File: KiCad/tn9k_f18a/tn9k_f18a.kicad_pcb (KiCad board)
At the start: 2 copper layers, 27.9 x 88.3 mm, 9 parts, among them J1 Conn_01x20, J2 Conn_01x20, J3 Conn_01x24, J4 Conn_01x24, J5 Conn_02x04_Counter_Clockwise, J6 Conn_02x08_Odd_Even, U1 SN74LVC245, U2 SN74LVC245, U3 SN74LVC245

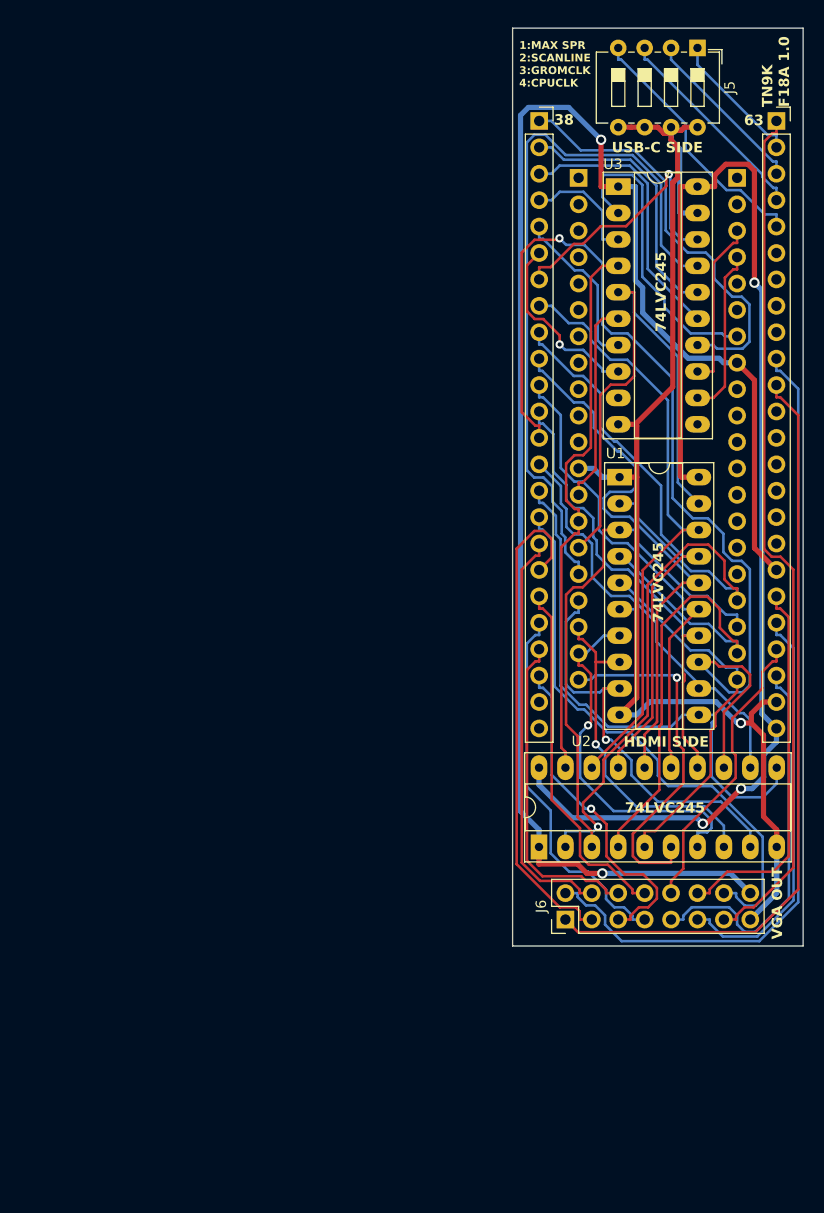
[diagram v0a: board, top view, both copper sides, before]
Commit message: SMD version
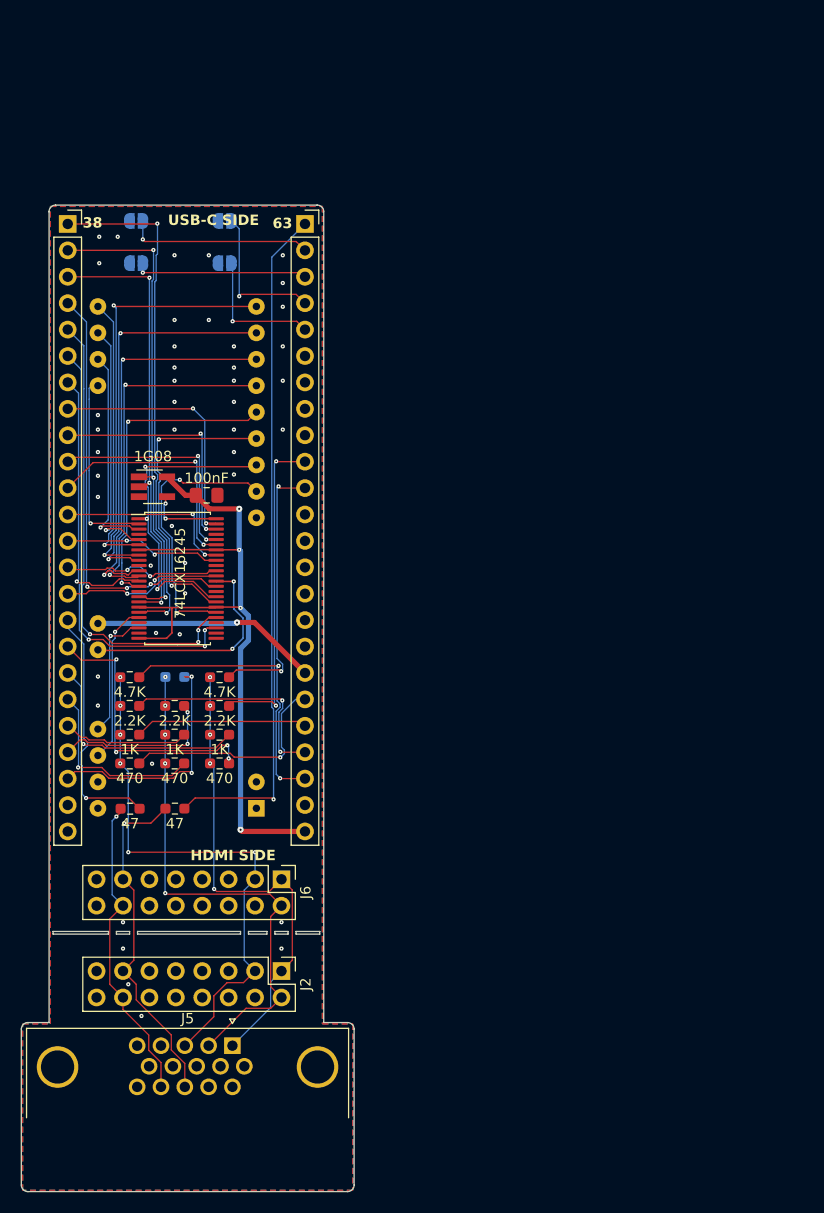
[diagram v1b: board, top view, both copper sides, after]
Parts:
- removed U2, U3: SN74LVC245, Package_DIP:DIP-20_W7.62mm_Socket_LongPads
- added C1: 100nF, Capacitor_SMD:C_0805_2012Metric_Pad1.18x1.45mm_HandSolder, F.Cu at (117.9, 86.2)
- added JP1: MAX SPR, Jumper:SolderJumper-2_P1.3mm_Open_RoundedPad1.0x1.5mm, B.Cu at (111.1, 59.8)
- added JP2: SCANLINE, Jumper:SolderJumper-2_P1.3mm_Open_RoundedPad1.0x1.5mm, B.Cu at (111.1, 63.9)
- added JP3: GROMCLK, Jumper:SolderJumper-2_P1.3mm_Open_RoundedPad1.0x1.5mm, B.Cu at (119.6, 59.8)
- added JP4: CPUCLK, Jumper:SolderJumper-2_P1.3mm_Open_RoundedPad1.0x1.5mm, B.Cu at (119.6, 63.9)
- added R1: 4.7K, Resistor_SMD:R_0603_1608Metric_Pad0.98x0.95mm_HandSolder, F.Cu at (119.1, 103.7)
- added R10: 2.2K, Resistor_SMD:R_0603_1608Metric_Pad0.98x0.95mm_HandSolder, F.Cu at (110.5, 106.5)
- added R11: 1K, Resistor_SMD:R_0603_1608Metric_Pad0.98x0.95mm_HandSolder, F.Cu at (110.5, 109.2)
- added R12: 470, Resistor_SMD:R_0603_1608Metric_Pad0.98x0.95mm_HandSolder, F.Cu at (110.5, 112.0)
- added R13: 47, Resistor_SMD:R_0603_1608Metric_Pad0.98x0.95mm_HandSolder, F.Cu at (114.8, 116.3)
- added R14: 47, Resistor_SMD:R_0603_1608Metric_Pad0.98x0.95mm_HandSolder, F.Cu at (110.5, 116.3)
- added R2: 2.2K, Resistor_SMD:R_0603_1608Metric_Pad0.98x0.95mm_HandSolder, F.Cu at (119.1, 106.5)
- added R3: 1K, Resistor_SMD:R_0603_1608Metric_Pad0.98x0.95mm_HandSolder, F.Cu at (119.1, 109.2)
- added R4: 470, Resistor_SMD:R_0603_1608Metric_Pad0.98x0.95mm_HandSolder, F.Cu at (119.1, 112.0)
- added R5: 4.7K, Resistor_SMD:R_0603_1608Metric_Pad0.98x0.95mm_HandSolder, B.Cu at (114.8, 103.7)
- added R6: 2.2K, Resistor_SMD:R_0603_1608Metric_Pad0.98x0.95mm_HandSolder, F.Cu at (114.8, 106.5)
- added R7: 1K, Resistor_SMD:R_0603_1608Metric_Pad0.98x0.95mm_HandSolder, F.Cu at (114.8, 109.2)
- added R8: 470, Resistor_SMD:R_0603_1608Metric_Pad0.98x0.95mm_HandSolder, F.Cu at (114.8, 112.0)
- added R9: 4.7K, Resistor_SMD:R_0603_1608Metric_Pad0.98x0.95mm_HandSolder, F.Cu at (110.5, 103.7)
- added U4: 74LCX16245, Package_SO:TSSOP-48_6.1x12.5mm_P0.5mm, F.Cu at (115.1, 94.2)
- J1: value Conn_01x20 -> ~; footprint Connector_PinHeader_2.54mm:PinHeader_1x20_P2.54mm_Vertical -> f18a_footprints:TMS99xxA_Replacement; moved to F.Cu
- J2: value Conn_01x20 -> VGA; footprint Connector_PinHeader_2.54mm:PinHeader_1x20_P2.54mm_Vertical -> Connector_PinHeader_2.54mm:PinHeader_2x08_P2.54mm_Vertical; moved to F.Cu
- J3: value Conn_01x24 -> Tang Nano 9k
- J4: value Conn_01x24 -> TN9k/2
- J5: value Conn_02x04_Counter_Clockwise -> VGA; footprint Button_Switch_THT:SW_DIP_SPSTx04_Slide_6.7x11.72mm_W7.62mm_P2.54mm_LowProfile -> Connector_Dsub:DSUB-15-HD_Female_Horizontal_P2.29x1.98mm_EdgePinOffset3.03mm_Housed_MountingHolesOffset4.94mm
- J6: value Conn_02x08_Odd_Even -> VGA
- U1: value SN74LVC245 -> 1G08; footprint Package_DIP:DIP-20_W7.62mm_Socket_LongPads -> Package_TO_SOT_SMD:SOT-23-5_HandSoldering
- moved J5 105.9 mm to (120.4, 139.1), turned to 0 degrees
- moved J2 88.0 mm to (125.1, 132.0), turned to -90 degrees
- moved J1 53.5 mm to (115.0, 92.7)
- moved J4 46.4 mm to (127.4, 60.1)
- moved J3 46.4 mm to (104.5, 60.1)
- moved U1 44.9 mm to (112.7, 85.4)
- moved J6 27.6 mm to (125.1, 123.1), turned to -90 degrees
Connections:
- J2 pad 1: unconnected-(J2-Pin_1-Pad1) -> RED
- J2 pad 10: unconnected-(J2-Pin_10-Pad10) -> GND
- J2 pad 13: unconnected-(J2-Pin_13-Pad13) -> HSYNC
- J2 pad 14: unconnected-(J2-Pin_14-Pad14) -> VSYNC
- J2 pad 2: unconnected-(J2-Pin_2-Pad2) -> GREEN
- J2 pad 3: CPUCLK -> BLUE
- J2 pad 4: GROMCLK -> unconnected-(J2-Pin_4-Pad4)
- J2 pad 5: COMVID -> GND
- J2 pad 6: EXTVDP -> GND
- J2 pad 7: ~{RESET} -> GND
- J2 pad 8: VCC -> GND
- J4 pad 18: VCC -> +5V
- J4 pad 24: VCC_3V3 -> +3.3V
- J5 pad 1: USR1_1V8 -> RED
- J5 pad 2: USR2_1V8 -> GREEN
- J5 pad 3: USR3_1V8 -> BLUE
- J5 pad 4: USR4_1V8 -> unconnected-(J5-Pad4)
- J6 pad 1: R0_3V3 -> RED
- J6 pad 10: B1_3V3 -> GND
- J6 pad 11: B2_3V3 -> unconnected-(J6-Pin_11-Pad11)
- J6 pad 12: B3_3V3 -> unconnected-(J6-Pin_12-Pad12)
- J6 pad 13: HS_3V3 -> HSYNC
- J6 pad 14: VS_3V3 -> VSYNC
- J6 pad 15: GND -> unconnected-(J6-Pin_15-Pad15)
- J6 pad 16: VCC -> unconnected-(J6-Pin_16-Pad16)
- J6 pad 2: R1_3V3 -> GREEN
- J6 pad 3: R2_3V3 -> BLUE
- J6 pad 4: R3_3V3 -> unconnected-(J6-Pin_4-Pad4)
- J6 pad 5: G0_3V3 -> GND
- J6 pad 6: G1_3V3 -> GND
- J6 pad 7: G2_3V3 -> GND
- J6 pad 8: G3_3V3 -> GND
- J6 pad 9: B0_3V3 -> unconnected-(J6-Pin_9-Pad9)
- U1 pad 1: GND -> ~{CSW_3V3}
- U1 pad 2: CD0 -> ~{CSR_3V3}
- U1 pad 3: CD1 -> GND
- U1 pad 4: CD2 -> ~{OE1}
- U1 pad 5: CD3 -> +3.3V
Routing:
- net VCC: track 156.4 -> 0.00 mm, vias 2 -> 0
- net VCC_3V3: track 124.9 -> 0.00 mm, vias 3 -> 0
- net GND: track 123.8 -> 0.00 mm, vias 1 -> 45
- net CD5_3V3: track 98.6 -> 15.2 mm, vias 1 -> 2
- net +3.3V: track 0.00 -> 71.4 mm, vias 0 -> 4
- net BLUE: track 0.00 -> 52.6 mm, vias 0 -> 6
- net GREEN: track 0.00 -> 51.1 mm, vias 0 -> 5
- net R1_3V3: track 79.9 -> 31.2 mm, vias 0 -> 2
- net R0_3V3: track 74.2 -> 26.1 mm, vias 0 -> 2
- net RED: track 0.00 -> 46.5 mm, vias 0 -> 5
- net CD0: track 62.0 -> 18.7 mm
- net ~{INT}: track 69.7 -> 30.3 mm, vias 0 -> 2
- net CD7_3V3: track 52.0 -> 15.6 mm, vias 0 -> 2
- net CD0_3V3: track 59.3 -> 24.6 mm, vias 0 -> 2
- net HSYNC: track 0.00 -> 33.3 mm, vias 0 -> 1
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- added copper zone on B.Cu, net GND
- added copper zone on F.Cu, net GND
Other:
- board size 27.9 x 88.3 mm -> 32 x 94.9 mm
- board text removed: "1"
- board text removed: "1:MAX SPR 2:SCANLINE 3:GROMCLK 4:CPUCLK"
- board text removed: "40"
- board text removed: "74LVC245"
- board text removed: "TMS91X8A"
- board text removed: "TN9K F18A 1.0"
- board text removed: "VGA OUT"
